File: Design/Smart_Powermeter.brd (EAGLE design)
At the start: 92 x 87 mm, 66 parts, among them IC1 AMS1117-3.3, IC3 ESP32-S2-MINI-1-N4R2, J1 AUDIO_JACK_TRRSSMD_RA, J2 AUDIO_JACK_TRRSSMD_RA, J3 AUDIO_JACK_TRRSSMD_RA, J4 AUDIO_JACK_TRRSSMD_RA, J5 AUDIO_JACK_TRRSSMD_RA, J6 AUDIO_JACK_TRRSSMD_RA, J8 USB-C, Q1 IRLML0100

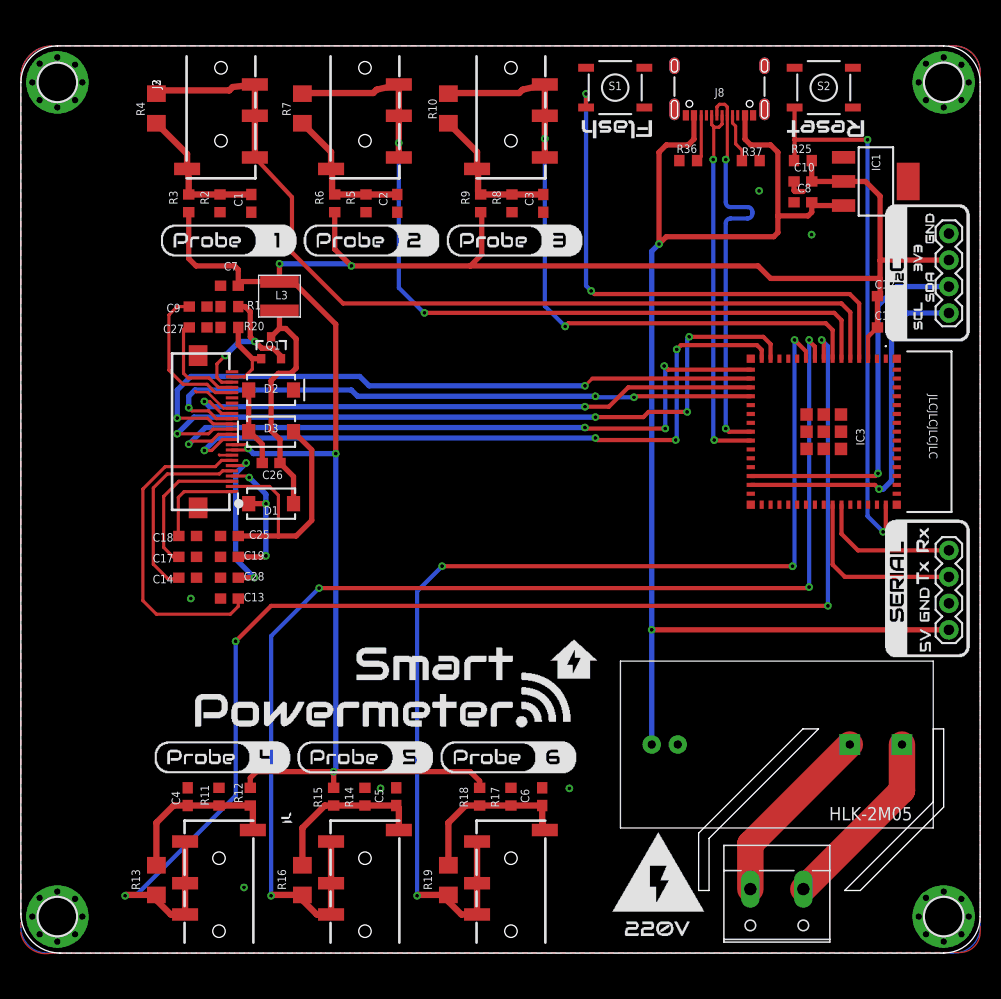
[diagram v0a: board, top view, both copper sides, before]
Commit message: Updated design files and silkscreen
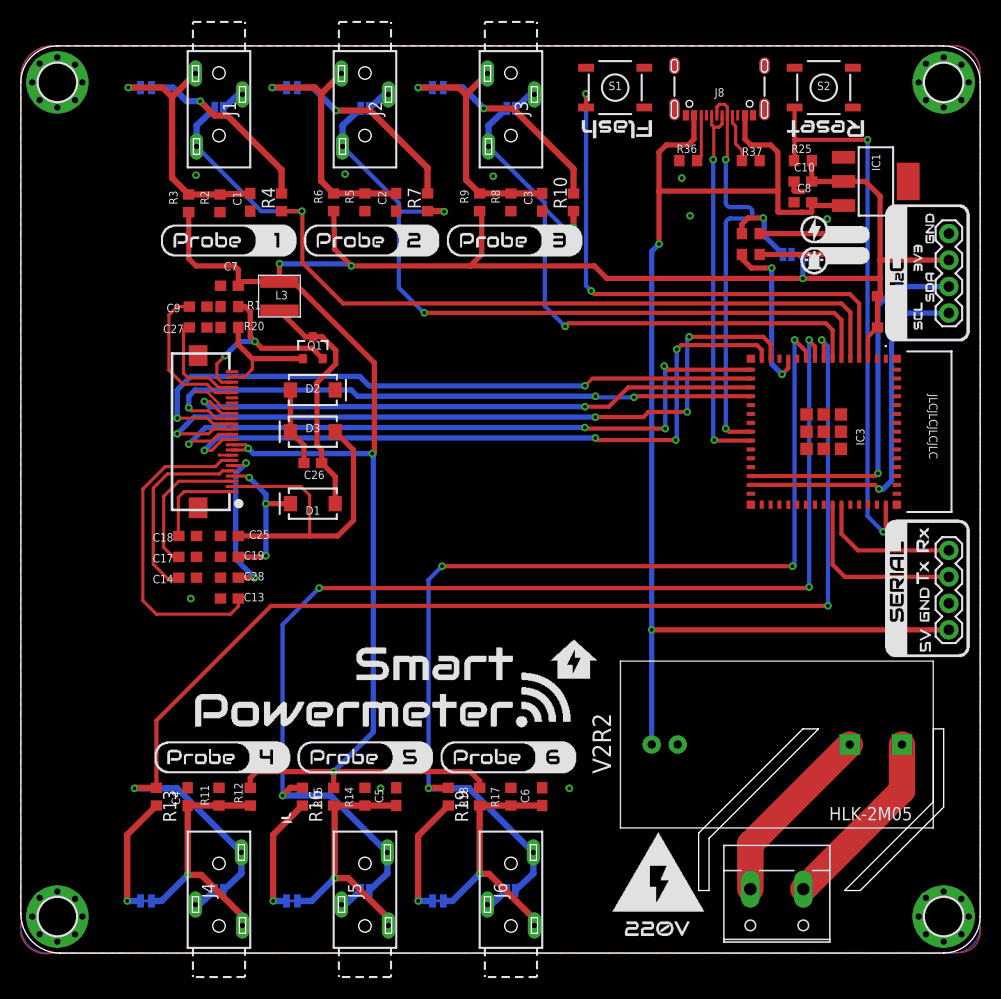
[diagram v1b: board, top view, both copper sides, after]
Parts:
- added JP1, JP2, JP3, JP4, JP5, JP6: JUMPER-SMT_2_NC_TRACE_NO-SILK, SparkFun-Jumpers:SMT-JUMPER_2_NC_TRACE_NO-SILK
- added JP10, JP11, JP12, JP7, JP8, JP9: JUMPER-SMT_2_NO_NO-SILK, SparkFun-Jumpers:SMT-JUMPER_2_NO_NO-SILK
- added JP13: JUMPER-SMT_2_NC_PASTE_NO-SILK, SparkFun-Jumpers:SMT-JUMPER_2_NC_PASTE_NO-SILK
- added LED1: GREEN, SparkFun-LED:LED-0603
- added LED2: BLUE, SparkFun-LED:LED-0603
- added R21: 330, rcl:R0603
- added R22: 470, rcl:R0603
- J1, J2, J3, J4, J5, J6: value AUDIO_JACK_TRRSSMD_RA -> AUDIO_JACK_MONO_3.5_3P; device SparkFun-Connectors:AUDIO_JACK_3.5MM_TRRS_SMD_RA -> SpaceDIY_connectors:HC-PJ-320A-3P-D
- R10, R13, R16, R19, R4, R7: device rcl:R1206 -> rcl:R0603
- R12, R15, R18, R3, R6, R9: value 10k -> 15k
- moved R10 15.0 mm to (53.0, 72.0)
- moved R4 15.0 mm to (25.0, 72.0)
- moved R7 15.0 mm to (39.0, 72.0)
- moved R13 8.00 mm to (13.0, 15.0)
- moved R16 8.00 mm to (27.0, 15.0)
- moved R19 8.00 mm to (41.0, 15.0)
- moved C26 4.00 mm to (28.0, 47.0)
- moved D1 4.00 mm to (28.0, 43.1)
- moved D2 4.00 mm to (28.0, 54.0)
- moved D3 4.00 mm to (28.0, 50.0)
- moved Q1 4.00 mm to (28.0, 58.0)
- moved J1 0.19 mm to (19.0, 86.5), turned to 180 degrees
- moved C1 0.14 mm to (22.0, 72.0)
- moved C2 0.14 mm to (36.0, 72.0)
- moved C3 0.14 mm to (50.0, 72.0)
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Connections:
- removed net VG0: C1.1, J1.EARTH, R2.2, R3.1, R4.1
- new net LED: IC3.12, R21.2
- new net N$10: J2.2, JP8.2
- new net N$18: J3.2, JP9.2
- new net N$19: J4.2, JP10.2
- new net N$20: J5.2, JP11.2
- new net N$21: J6.2, JP12.2
- new net N$22: JP13.2, R22.2
- new net N$29: LED2.A, R21.1
- new net N$3: JP1.2, R4.2
- new net N$33: LED1.A, R22.1
- new net N$4: JP2.2, R7.2
- new net N$5: JP3.2, R10.2
- new net N$6: JP4.2, R13.2
- new net N$7: JP5.2, R16.2
- new net N$8: JP6.2, R19.2
- new net N$9: J1.2, JP7.2
- new net VG6: C6.1, J6.1, JP6.1, R17.2, R18.1
- net 3.3V: now also JP13.1
- net GND: now also LED1.C, LED2.C
- net M1: now also J1.3, JP7.1, R4.1; no longer J1.RING1, J1.RING2, J1.TIP, R4.2
- net M2: now also J2.3, JP8.1, R7.1; no longer J2.RING1, J2.RING2, J2.TIP, R7.2
- net M3: now also J3.3, JP9.1, R10.1; no longer J3.RING1, J3.RING2, J3.TIP, R10.2
- net M4: now also J4.3, JP10.1, R13.1; no longer J4.RING1, J4.RING2, J4.TIP, R13.2
- net M5: now also J5.3, JP11.1, R16.1; no longer J5.RING1, J5.RING2, J5.TIP, R16.2
- net M6: now also J6.3, JP12.1, R19.1; no longer J6.RING1, J6.RING2, J6.TIP, R19.2
- net VG1: now also C1.1, J1.1, JP1.1, R2.2, R3.1; no longer C2.1, J2.EARTH, R5.2, R6.1, R7.1
- net VG2: now also C2.1, J2.1, JP2.1, R5.2, R6.1; no longer C3.1, J3.EARTH, R10.1, R8.2, R9.1
- net VG3: now also C3.1, J3.1, JP3.1, R8.2, R9.1; no longer C4.1, J4.EARTH, R11.2, R12.1, R13.1
- net VG4: now also C4.1, J4.1, JP4.1, R11.2, R12.1; no longer C5.1, J5.EARTH, R14.2, R15.1, R16.1
- net VG5: now also C5.1, J5.1, JP5.1, R14.2, R15.1; no longer C6.1, J6.EARTH, R17.2, R18.1, R19.1
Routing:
- net VG6: track 0.00 -> 25.4 mm, vias 0 -> 1
- net N$4: track 0.00 -> 18.1 mm, vias 0 -> 1
- net N$5: track 0.00 -> 18.1 mm, vias 0 -> 1
- net N$3: track 0.00 -> 17.8 mm, vias 0 -> 1
- net LED: track 0.00 -> 16.0 mm, vias 0 -> 2
- net VG0: track 14.1 -> 0.00 mm
- net N$8: track 0.00 -> 11.7 mm, vias 0 -> 1
- net N$6: track 0.00 -> 11.6 mm, vias 0 -> 1
- net N$7: track 0.00 -> 11.6 mm, vias 0 -> 1
- net VG2: track 14.1 -> 25.3 mm, vias 0 -> 1
- net VG1: track 14.1 -> 24.8 mm, vias 0 -> 1
- net 3.3V: track 206.4 -> 216.7 mm, vias 5 -> 6
- net VG4: track 15.9 -> 26.1 mm, vias 0 -> 1
- net VG3: track 16.2 -> 25.4 mm, vias 0 -> 1
- net VG5: track 16.2 -> 24.9 mm, vias 0 -> 1
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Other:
- board text added: "V2R2"
